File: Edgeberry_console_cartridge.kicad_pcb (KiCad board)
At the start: 2 copper layers, 49.8 x 63.2 mm, 84 parts, among them J1 USB_B, J3 Screw_Terminal_01x03, U1 FT232RL, U2 MCP2515, U3 MCP2562, Y1 16MHz

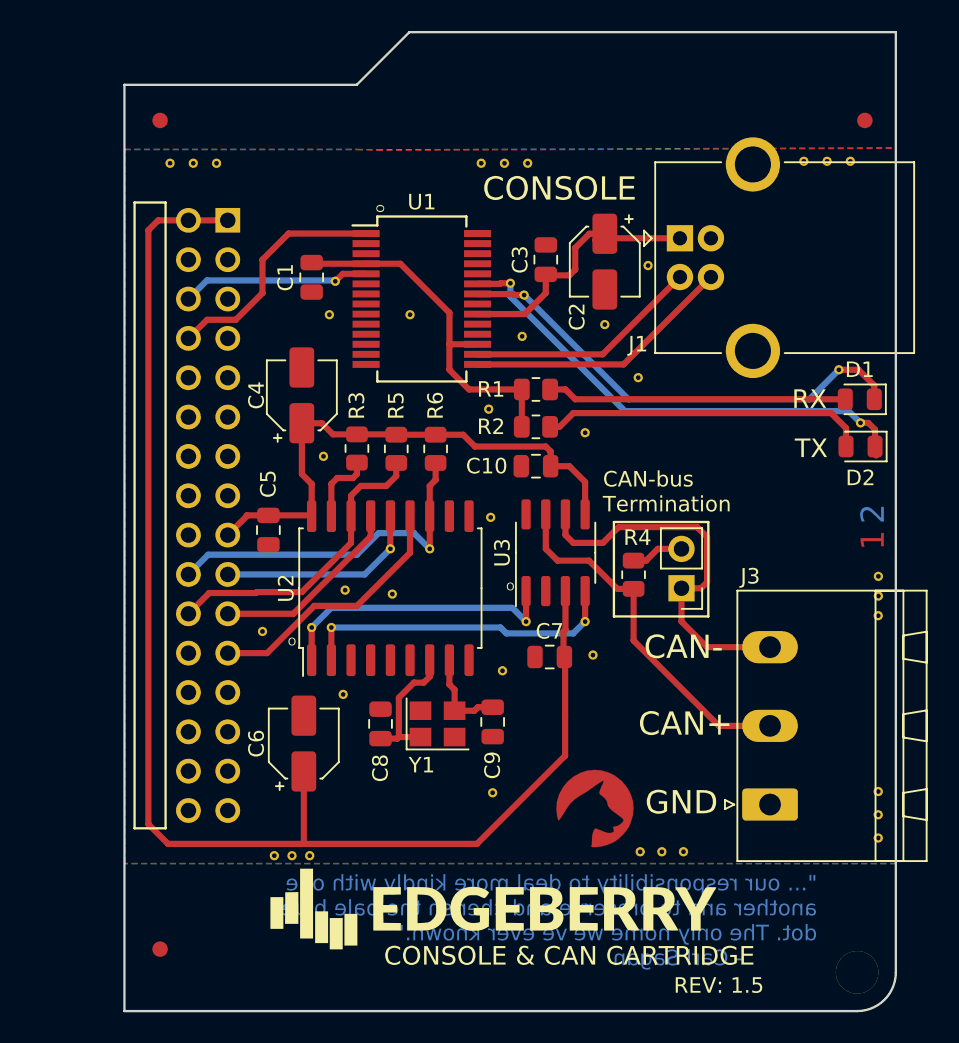
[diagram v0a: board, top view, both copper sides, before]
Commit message: Update to KiCad 8 + footprint cleanup
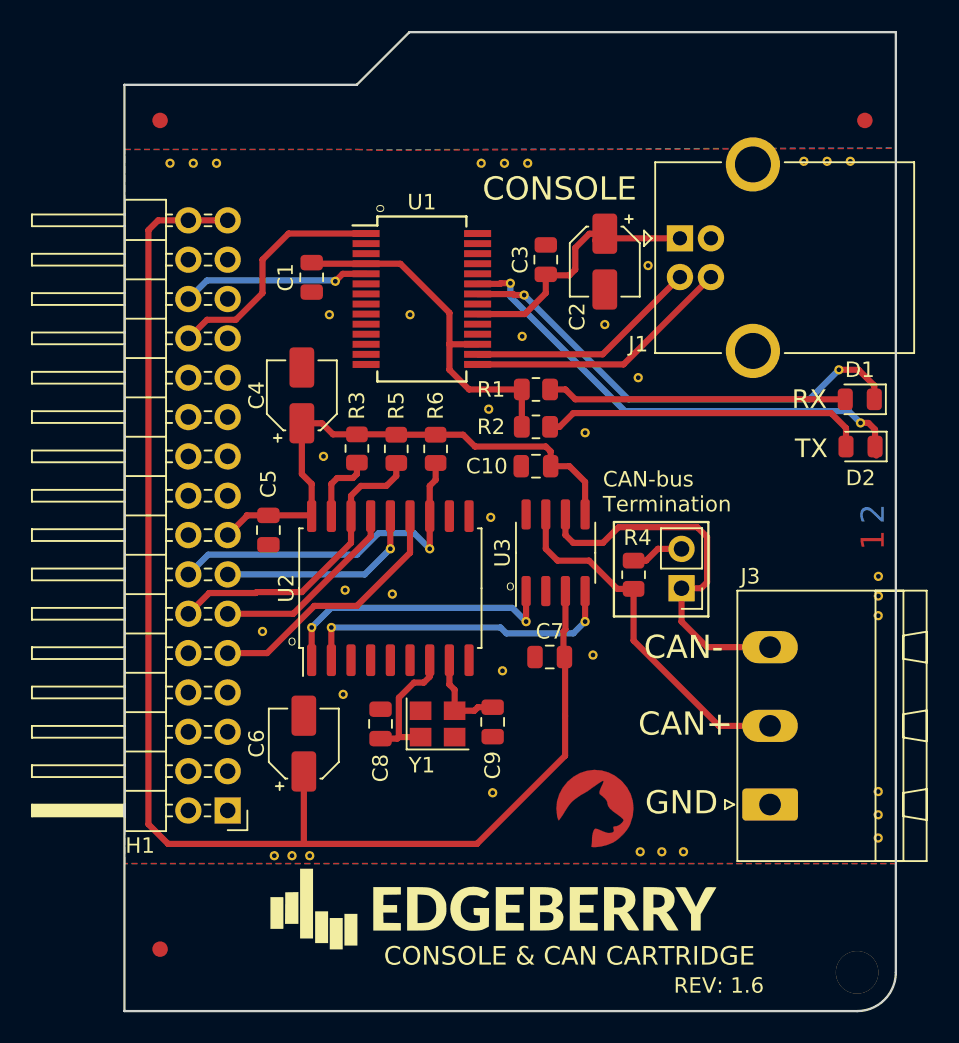
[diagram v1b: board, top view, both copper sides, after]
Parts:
- added G***: LOGO, LOGO, B.Cu at (171.7, 104.2)
- added G***: LOGO, LOGO, B.Cu at (171.7, 109.8)
- added G***: LOGO, LOGO, B.Cu at (171.8, 99.2)
- H1: value EdgeBerry_IO -> Edgeberry_Cartridge_Header; footprint emcosys:EdgeBerry_IO_male -> Connector_PinHeader_2.54mm:PinHeader_2x16_P2.54mm_Horizontal
- moved H1 19.1 mm to (131.9, 122.0), turned to 180 degrees
- moved G*** 4.38 mm to (145.3, 105.5)
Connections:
- H1 pad 1: +5V -> unconnected-(H1-3v3_PWR-Pad1)
- H1 pad 11: unconnected-(H1-Pad11) -> SPI_MISO
- H1 pad 12: GND -> SPI_CS0
- H1 pad 13: unconnected-(H1-Pad13) -> SPI_MOSI
- H1 pad 14: unconnected-(H1-Pad14) -> INT
- H1 pad 15: unconnected-(H1-Pad15) -> +3V3
- H1 pad 16: unconnected-(H1-Pad16) -> GND
- H1 pad 17: +3V3 -> unconnected-(H1-GPIO_22-Pad17)
- H1 pad 18: GND -> unconnected-(H1-GPIO_24-Pad18)
- H1 pad 19: SPI_MOSI -> unconnected-(H1-GPIO_27-Pad19)
- H1 pad 2: +5V -> unconnected-(H1-GPIO_21-Pad2)
- H1 pad 20: INT -> unconnected-(H1-GPIO_23-Pad20)
- H1 pad 21: SPI_MISO -> unconnected-(H1-GPIO_17-Pad21)
- H1 pad 22: SPI_CS0 -> GND
- H1 pad 23: SPI_SCL -> GND
- H1 pad 25: GND -> unconnected-(H1-GPIO_4-Pad25)
- H1 pad 26: unconnected-(H1-Pad26) -> UART_RX
- H1 pad 28: GND -> UART_TX
- H1 pad 30: unconnected-(H1-Pad30) -> GND
- H1 pad 31: unconnected-(H1-Pad31) -> +5V
- H1 pad 32: unconnected-(H1-Pad32) -> +5V
- H1 pad 4: GND -> unconnected-(H1-GPIO_16-Pad4)
- H1 pad 6: UART_TX -> GND
- H1 pad 7: unconnected-(H1-Pad7) -> GND
- H1 pad 8: UART_RX -> unconnected-(H1-GND-Pad8)
- H1 pad 9: GND -> SPI_SCL
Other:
- board text added: "Console & CAN Cartridge"
- board text added: "EDGEBERRY"
- board text added: "REV: 1.6"
- board text removed: "15.0mm"
- board text removed: "3.4mm"
- board text removed: "31.4mm"
- board text removed: "59.8mm"
- board text removed: "6.60mm"
- board text removed: "63.2mm"
- board text removed: "8.76mm"
- board text removed: "EdgeBerry Cartridge"
- board text removed: "KEEP AREA CLEAR"
- board text removed: "REV: 1.5"
- board text removed: "{dblquote}... our responsibility to deal more kindly with one another and to preserve and cherish the pale blue dot. The only home we've ever known.{dblquote} - Carl Sagan"

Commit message: Silk screen improvements
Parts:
- removed the G*** at (149.2, 128.4)
- removed the G*** at (145.3, 105.5)
- removed the G*** at (171.8, 99.2)
- added G***: LOGO, LOGO, F.Cu at (151.0, 127.5)
- added G***: LOGO, LOGO, F.Cu at (136.1, 128.5)
- added G***: LOGO, LOGO, B.Cu at (171.8, 85.9)
- added G***: LOGO, LOGO, B.Cu at (141.9, 103.0)
- moved G*** 28.3 mm to (171.7, 81.5)
- moved G*** 19.3 mm to (171.8, 95.3)
- moved G*** 13.6 mm to (171.8, 90.6)
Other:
- board text removed: "O"

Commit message: Open Source Hardware license: CERN-OHL-W
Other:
- board text added: "Copyright© 2024 Sanne 'SpuQ' Santens. This design is released under the CERN OHL-W license on GitHub."
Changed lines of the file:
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@@
 		)
 		(fp_text user "${REFERENCE}"
-			(at 5.31 19.05 270)
+			(at 5.31 19.05 -90)
 			(layer "F.Fab")
 			(effects
@@
 	)
 	(gr_text "REV.: 1.5, Mid 2024"
-		(at 107.05 55.95 0)
+		(at 107 50 0)
 		(layer "Dwgs.User")
 		(effects
@@
 	)
 	(gr_text "EDGEBERRY"
-		(at 106.35 40.3 0)
+		(at 106.35 36 0)
 		(layer "Dwgs.User")
 		(effects
@@
 	)
 	(gr_text "Console & CAN Cartridge\n"
-		(at 106.55 48.45 0)
+		(at 106.55 44 0)
 		(layer "Dwgs.User")
 		(effects
@@
 		)
 	)
+	(gr_text "Copyright© 2024 Sanne 'SpuQ' Santens. This design is released under\nthe CERN OHL-W license on GitHub."
+		(at 107 57 0)
+		(layer "Dwgs.User")
+		(effects
+			(font
+				(size 1.5 1.5)
+				(thickness 0.2)
+				(bold yes)
+			)
+			(justify left bottom)
+		)
+	)
 	(dimension
 		(type aligned)
@@
 		)
 		(height 4.85)
-		(gr_text "3,4 mm"
+		(gr_text "3.4 mm"
 			(at 143.95 64.65 0)
 			(layer "Dwgs.User")
@@
 		)
 		(height -12.975)
-		(gr_text "59,8 mm"
+		(gr_text "59.8 mm"
 			(at 110.425 105.1 90)
 			(layer "Dwgs.User")
